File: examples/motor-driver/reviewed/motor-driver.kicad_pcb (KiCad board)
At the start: 2 copper layers, 88 x 50 mm, 15 parts, among them J1 VM 2.7-10.8V, J2 MOTOR A, J3 MOTOR B, J4 LOGIC, U1 DRV8833PW

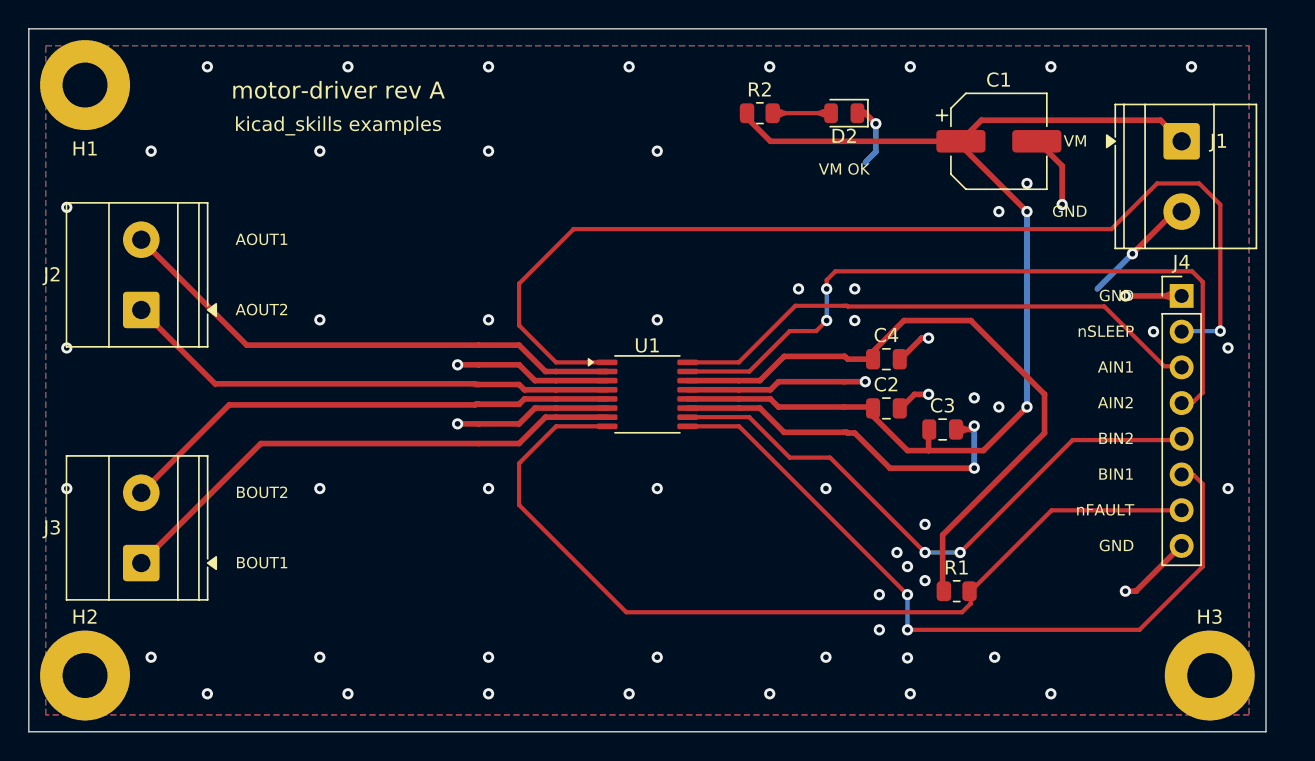
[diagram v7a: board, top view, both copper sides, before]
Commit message: Give the assembly machine something to aim at
Fiducials: three copper dots in bare mask windows, near three different
corners so a pick-and-place gets rotation as well as offset. It aligns
to the board, not to the drawing - without them it has only the routed
outline, cut to a tolerance ten times looser than the placement a 0.5 mm
pitch part is asking for. `fab.no_fiducials` reports a fine-pitch board
that has none, as context rather than as a fault: plenty of boards are
built one at a time with tweezers.

They share the corner search with the mounting holes, which is where
this found a real bug: `_courtyard_box` read lines and rectangles only,
and a mounting hole draws its courtyard as one circle - so every hole
measured as taking up no room at all, and the first three fiducials
landed on top of three screw holes. Circles and arcs count now.

Co-Authored-By: Claude Fable 5 <noreply@anthropic.com>
Claude-Session: https://claude.ai/code/session_01DUj7Ltu92tWg159mCSacwY
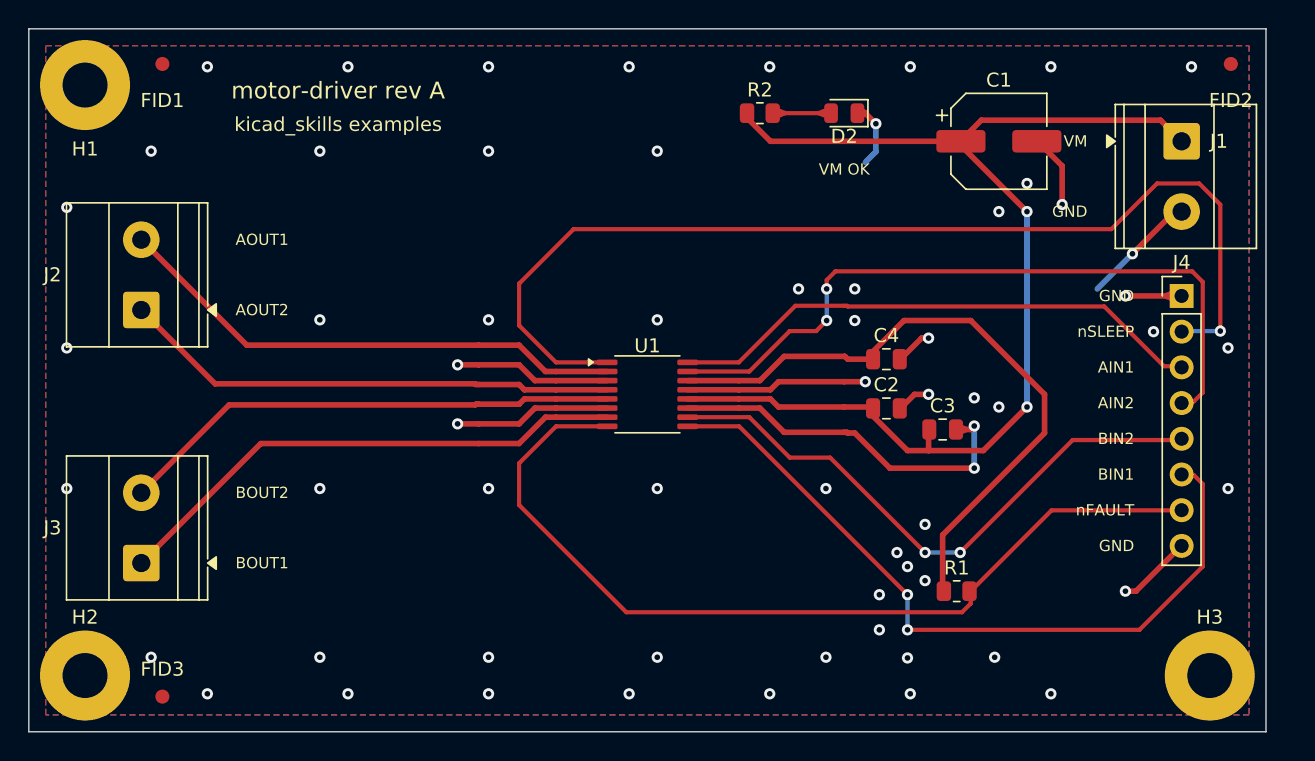
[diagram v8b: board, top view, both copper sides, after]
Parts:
- added FID1: Fiducial, Fiducial:Fiducial_1mm_Mask2mm, F.Cu at (109.5, 62.5)
- added FID2: Fiducial, Fiducial:Fiducial_1mm_Mask2mm, F.Cu at (185.5, 62.5)
- added FID3: Fiducial, Fiducial:Fiducial_1mm_Mask2mm, F.Cu at (109.5, 107.5)
- H1, H2, H3: value M33 -> M3
